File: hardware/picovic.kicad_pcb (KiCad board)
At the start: 2 copper layers, 54.6 x 53.3 mm, 18 parts, among them J1 DB15_Female_HighDensity, J2 Conn_01x06, P1 Mini-DIN_6pins_ver2, U1 74HC14

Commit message: Set variables
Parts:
- moved R10 124.7 mm to (156.2, 103.1)
- moved P1 124.7 mm to (169.3, 116.2)
- moved U1 124.7 mm to (162.4, 91.8)
- moved C1 124.7 mm to (154.3, 95.1)
- moved C2 124.7 mm to (154.3, 98.4)
- moved J1 124.7 mm to (167.3, 87.5)
- moved J2 124.7 mm to (162.4, 107.3)
- moved R1 124.7 mm to (151.0, 75.3)
- moved R2 124.7 mm to (151.0, 78.6)
- moved R3 124.7 mm to (151.0, 81.9)
- moved R4 124.7 mm to (151.0, 85.2)
- moved R5 124.7 mm to (151.0, 88.5)
- moved R6 124.7 mm to (151.0, 91.8)
- moved R7 124.7 mm to (151.0, 95.1)
- moved R8 124.7 mm to (151.0, 98.4)
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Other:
- board text added: "REV: ${VERSION}"

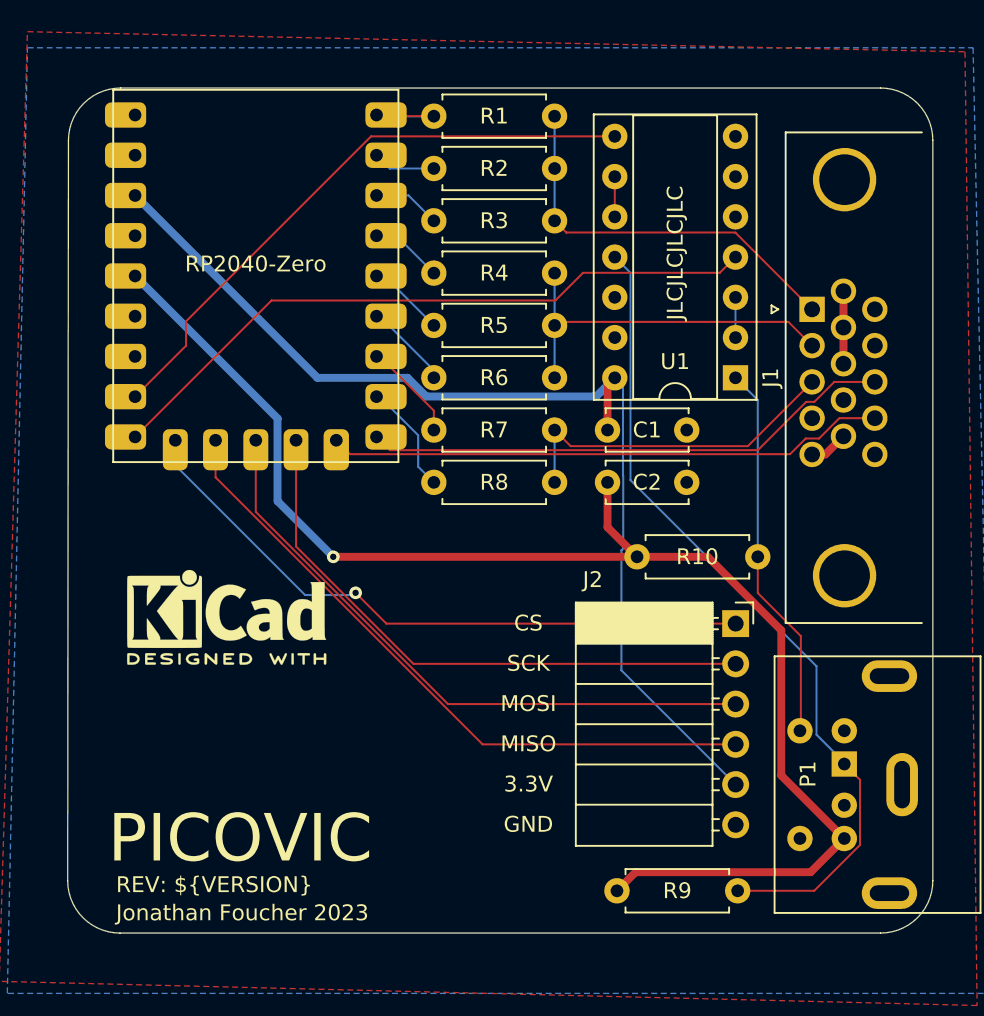
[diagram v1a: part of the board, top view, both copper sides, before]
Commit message: Fix i2c pins order
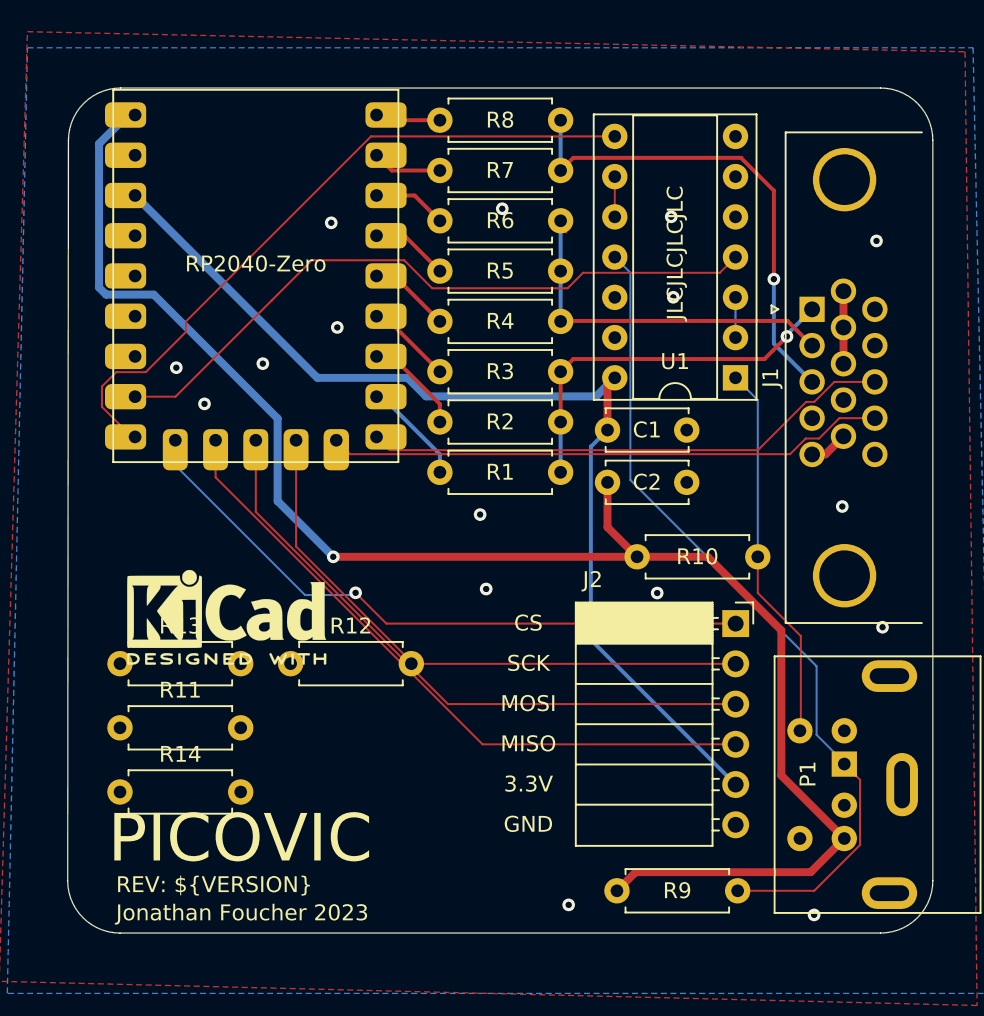
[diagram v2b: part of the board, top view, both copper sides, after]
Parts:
- added R11: 250R, Resistor_THT:R_Axial_DIN0207_L6.3mm_D2.5mm_P7.62mm_Horizontal, F.Cu at (123.6, 113.9)
- added R12: 250R, Resistor_THT:R_Axial_DIN0207_L6.3mm_D2.5mm_P7.62mm_Horizontal, F.Cu at (134.3, 109.9)
- added R13: 250R, Resistor_THT:R_Axial_DIN0207_L6.3mm_D2.5mm_P7.62mm_Horizontal, F.Cu at (123.6, 109.9)
- added R14: 250R, Resistor_THT:R_Axial_DIN0207_L6.3mm_D2.5mm_P7.62mm_Horizontal, F.Cu at (123.6, 118.0)
- R10, R9: value R -> 2k
- moved R8 22.9 mm to (151.4, 75.6)
- moved R1 22.5 mm to (151.4, 97.8)
- moved R7 16.4 mm to (151.4, 78.7)
- moved R2 16.0 mm to (151.4, 94.6)
- moved R6 9.91 mm to (151.4, 81.9)
- moved R3 9.53 mm to (151.4, 91.4)
- moved R5 3.45 mm to (151.4, 85.1)
- moved R4 3.07 mm to (151.4, 88.3)
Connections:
- net Net-(P1-Pad1) renamed /PS2_DATA
- net Net-(P1-Pad5) renamed /PS2_CLK
- R1 pad 2: Net-(R1-Pad2) -> Net-(RZ1-Pad8)
- R2 pad 2: Net-(R2-Pad2) -> Net-(RZ1-Pad7)
- RZ1 pad 1: Net-(R1-Pad2) -> Net-(R8-Pad2)
- RZ1 pad 15: Net-(RZ1-Pad15) -> /CS
- RZ1 pad 17: unconnected-(RZ1-Pad17) -> Net-(RZ1-Pad17)
- RZ1 pad 18: unconnected-(RZ1-Pad18) -> Net-(RZ1-Pad18)
- RZ1 pad 19: unconnected-(RZ1-Pad19) -> Net-(RZ1-Pad19)
- RZ1 pad 2: Net-(R2-Pad2) -> Net-(R7-Pad2)
- RZ1 pad 20: unconnected-(RZ1-Pad20) -> Net-(RZ1-Pad20)
- RZ1 pad 22: +5V -> GND
- RZ1 pad 23: GND -> +5V
- RZ1 pad 3: Net-(R3-Pad2) -> Net-(R6-Pad2)
- RZ1 pad 4: Net-(R4-Pad2) -> Net-(R5-Pad2)
- RZ1 pad 5: Net-(R5-Pad2) -> Net-(R4-Pad2)
- RZ1 pad 6: Net-(R6-Pad2) -> Net-(R3-Pad2)
- RZ1 pad 7: Net-(R7-Pad2) -> Net-(RZ1-Pad7)
- RZ1 pad 8: Net-(R8-Pad2) -> Net-(RZ1-Pad8)
- U1 pad 4: Net-(RZ1-Pad15) -> Net-(RZ1-Pad16)
- U1 pad 8: Net-(RZ1-Pad16) -> /CS
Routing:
- net /CS: track 41.5 -> 85.0 mm
- net Net-(RZ1-Pad15): track 42.6 -> 0.00 mm
- net +5V: track 89.1 -> 103.2 mm
- net Net-(J1-Pad3): track 21.7 -> 30.9 mm, vias 0 -> 1
- net Net-(R1-Pad2): track 7.30 -> 0.00 mm
- net Net-(RZ1-Pad8): track 0.00 -> 6.64 mm
- net Net-(RZ1-Pad7): track 0.00 -> 6.38 mm
- net Net-(RZ1-Pad16): track 38.0 -> 43.0 mm
- net Net-(R2-Pad2): track 3.97 -> 0.00 mm
- net Net-(R8-Pad2): track 6.83 -> 4.35 mm
- net Net-(R5-Pad2): track 4.42 -> 6.18 mm
- net +3.3V: track 68.4 -> 66.8 mm
- net Net-(R6-Pad2): track 5.30 -> 6.68 mm
- net Net-(R3-Pad2): track 4.28 -> 5.45 mm
- net Net-(J1-Pad1): track 25.2 -> 24.0 mm, vias 0 -> 1
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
